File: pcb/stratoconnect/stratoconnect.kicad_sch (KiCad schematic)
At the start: 7 parts

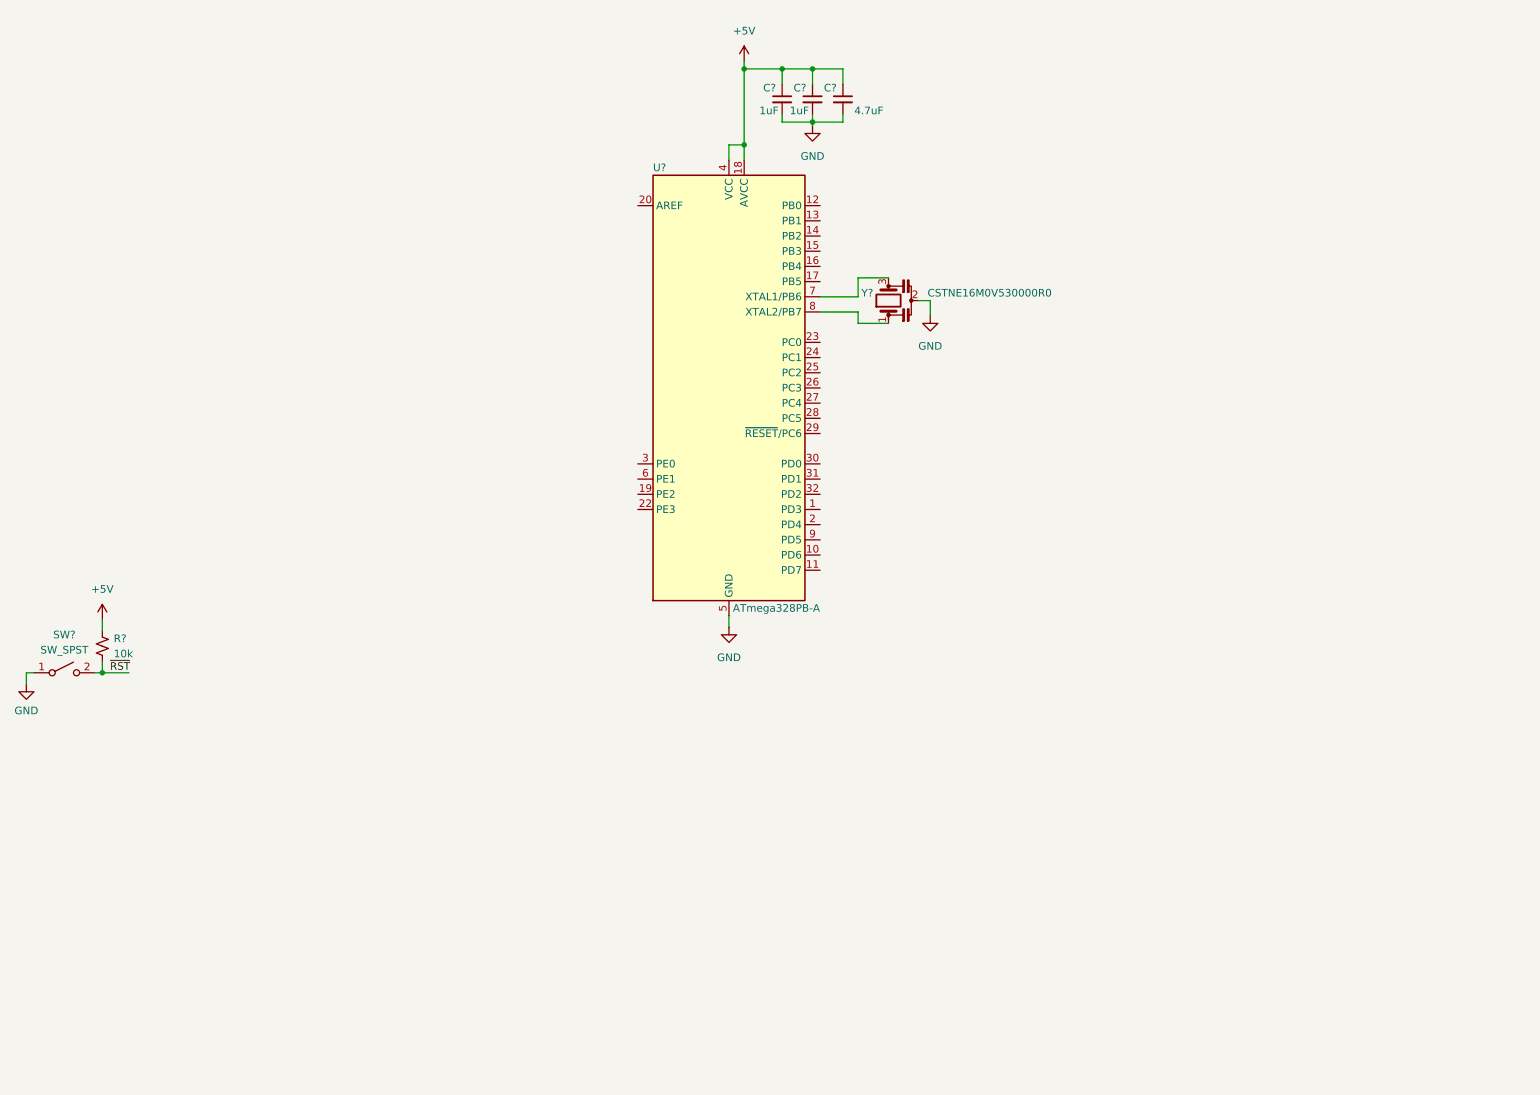
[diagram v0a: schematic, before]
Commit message: draw out the base schematic with the RF module
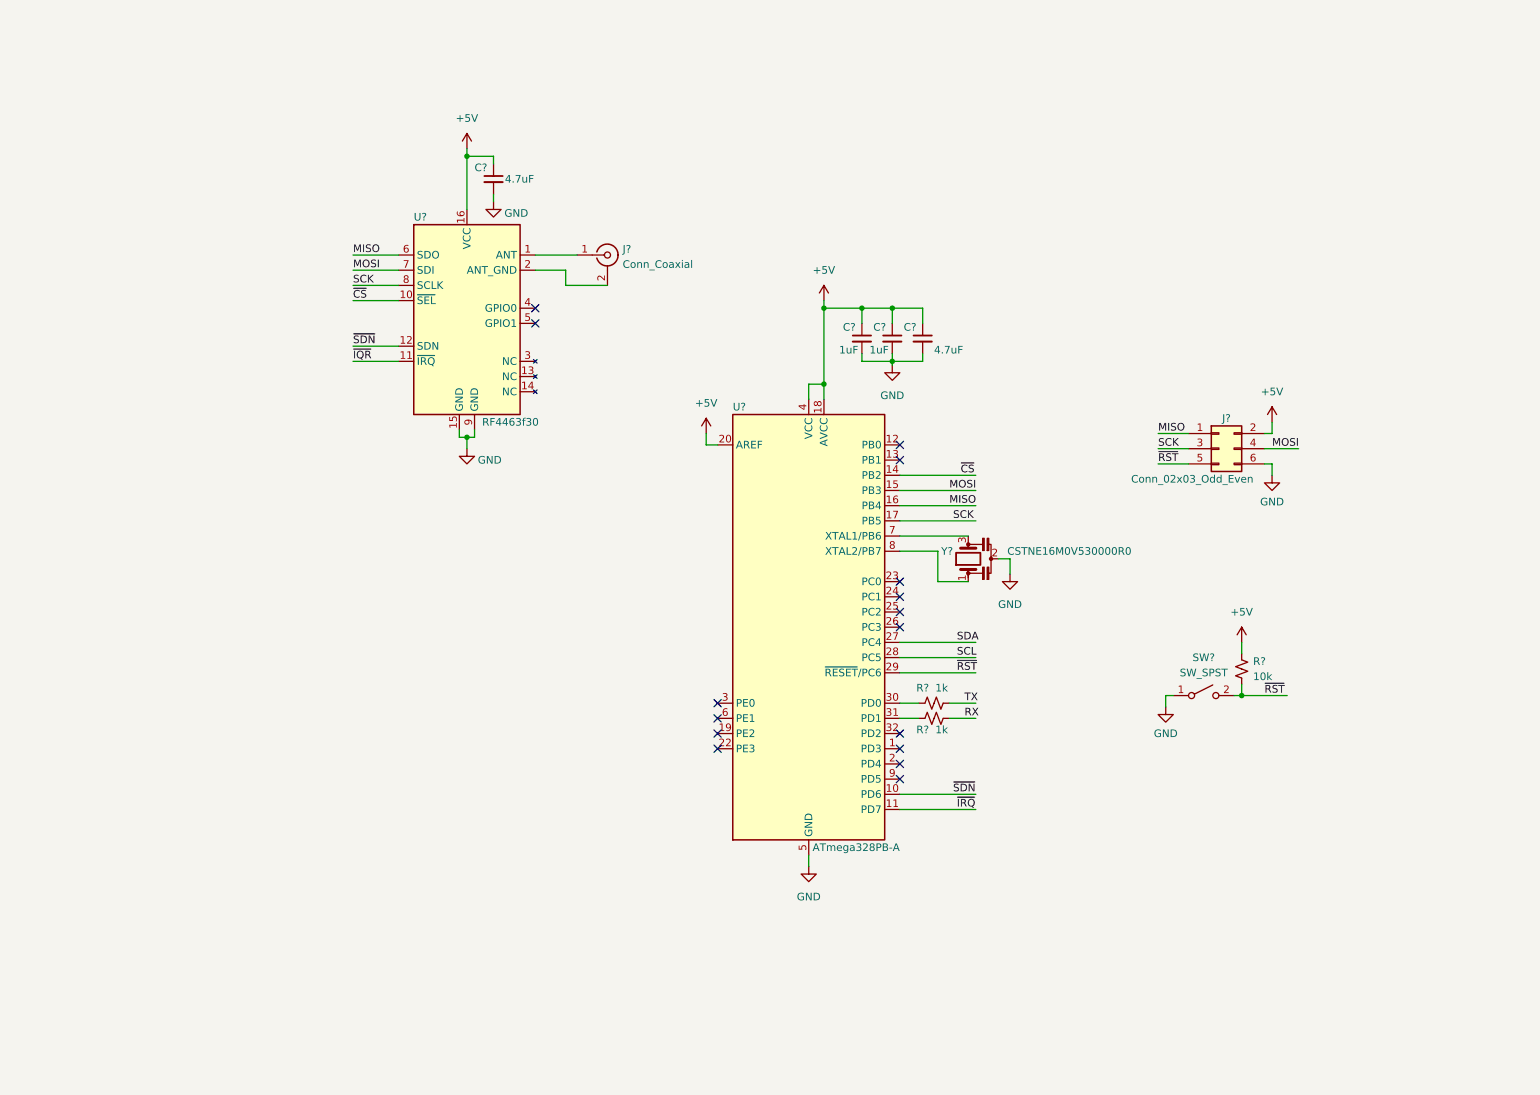
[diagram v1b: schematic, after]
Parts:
- added C?: 4.7uF, Capacitor_SMD:C_0603_1608Metric, symbol Device:C_Small
- added J?: Conn_02x03_Odd_Even, Connector_PinHeader_2.54mm:PinHeader_2x03_P2.54mm_Vertical, symbol Connector_Generic:Conn_02x03_Odd_Even
- added J?: Conn_Coaxial, symbol Connector:Conn_Coaxial
- added R? (x2): 1k, Resistor_SMD:R_0603_1608Metric, symbol Device:R_Small_US
- added U?: RF4463f30, RF:RF4463F30, symbol RF_Module:RF4463f30
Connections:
- net +5V: now also U?.20 (AREF), C?.1, J?.2 (Pin_2), U?.16 (VCC)
- net GND: now also C?.2, J?.6 (Pin_6), U?.15 (GND), U?.9 (GND)
- net ~{RST}: now also U?.29 (~{RESET}/PC6), J?.5 (Pin_5)
- net ~{SDN}: now reaches U?.10 (PD6)
- net ~{SDN}: now also U?.12 (SDN)
- net ~{IRQ}: now reaches U?.11 (PD7)
- net ~{CS}: now reaches U?.14 (PB2)
- net ~{CS}: now also U?.10 (~{SEL})
- net MOSI: now reaches U?.15 (PB3)
- net MOSI: now also J?.4 (Pin_4), U?.7 (SDI)
- net MISO: now reaches U?.16 (PB4)
- net MISO: now also J?.1 (Pin_1), U?.6 (SDO)
- net SCK: now reaches U?.17 (PB5)
- net SCK: now also J?.3 (Pin_3), U?.8 (SCLK)
- net SDA: now reaches U?.27 (PC4)
- net SCL: now reaches U?.28 (PC5)
- net at U?.30 (PD0): now also R?.1
- net at U?.31 (PD1): now also R?.1
- new net: J?.1 (In), U?.1 (ANT)
- new net: J?.2 (Ext), U?.2 (ANT_GND)
- new net RX: R?.2
- new net TX: R?.2
- new net ~{IQR}: U?.11 (~{IRQ})
- no-connect marks 0 -> 16
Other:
- moved on the sheet: C?, R?, SW?, U?, Y?

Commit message: add rough margin
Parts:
- added J3: Conn_01x05_Male, Connector_JST:JST_GH_BM05B-GHS-TBT_1x05-1MP_P1.25mm_Vertical, symbol Connector:Conn_01x05_Male
- added J4: Conn_01x02_Male, Connector_JST:JST_EH_S2B-EH_1x02_P2.50mm_Horizontal, symbol Connector:Conn_01x02_Male
- added J5: Conn_01x03_Male, Connector_JST:JST_GH_BM03B-GHS-TBT_1x03-1MP_P1.25mm_Vertical, symbol Connector:Conn_01x03_Male
- J1: renamed from J?; footprint (none) -> Connector_Coaxial:SMA_Molex_73251-2120_EdgeMount_Horizontal
- gave numbers to parts that had none: 12
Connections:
- net +5V: now also J4.1 (Pin_1)
- net GND: now also J3.5 (Pin_5), J4.2 (Pin_2), J5.2 (Pin_2)
- net RX: now also J5.1 (Pin_1)
- net SCL: now also J3.2 (Pin_2)
- net SDA: now also J3.3 (Pin_3)
- net TX: now also J5.3 (Pin_3)
- new net +3V3: J3.4 (Pin_4)
- new net ~{INT}: J3.1 (Pin_1)

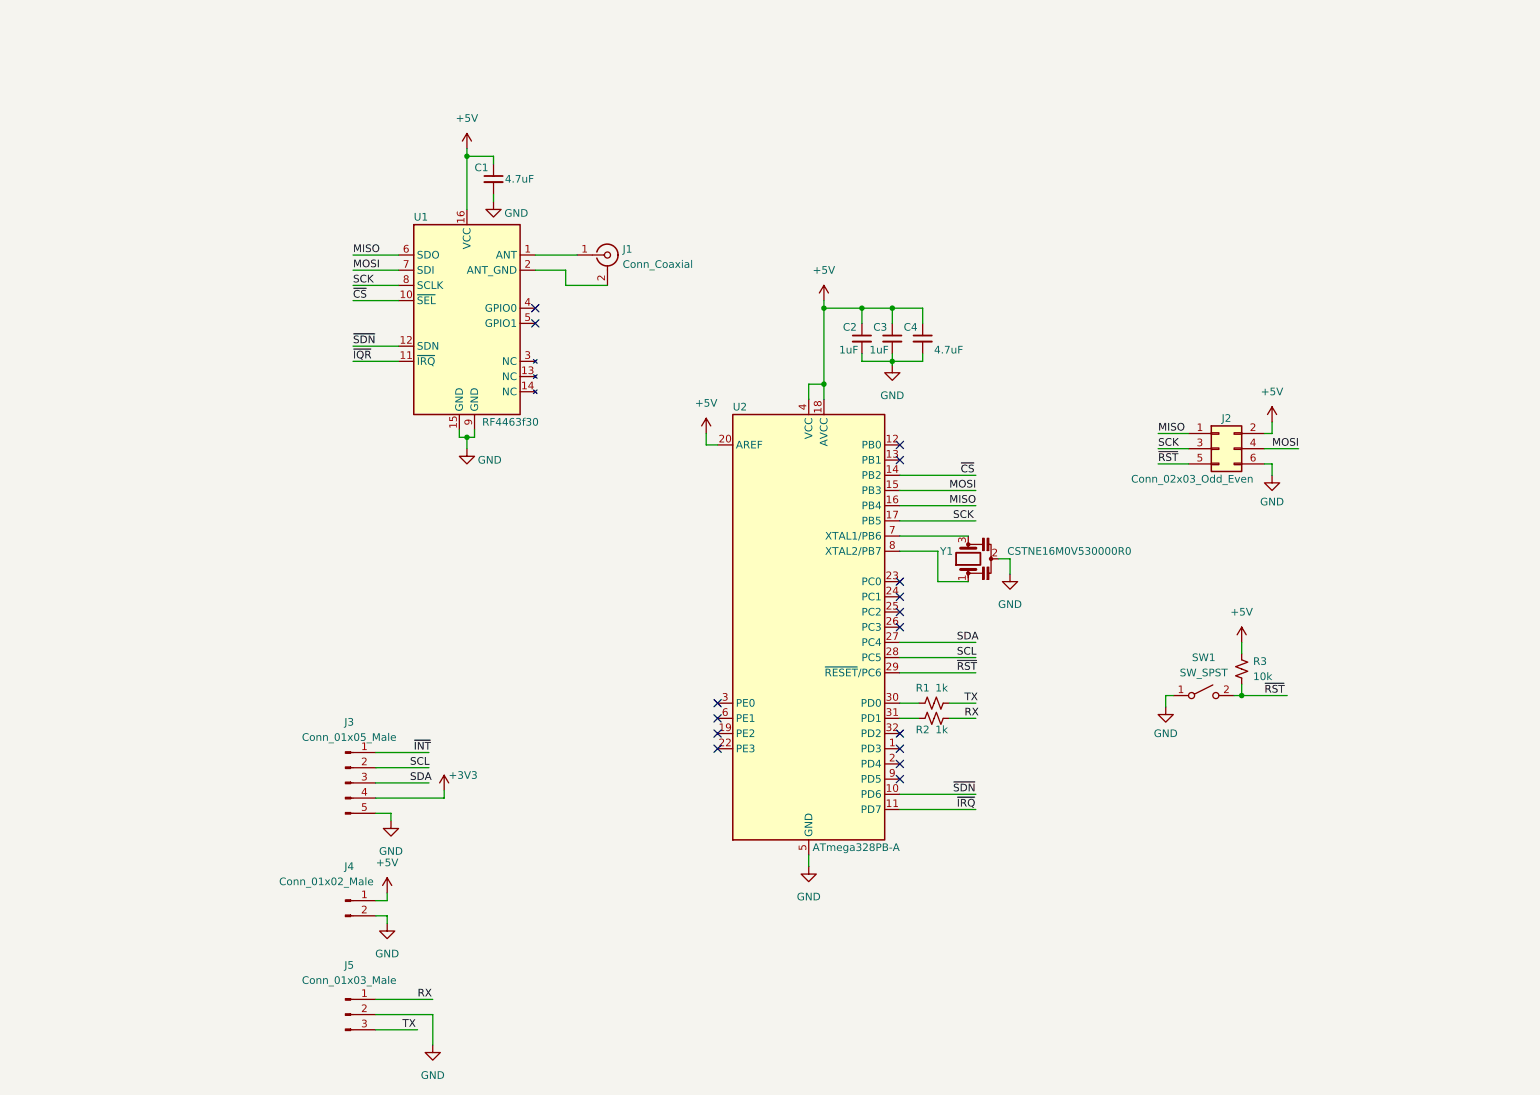
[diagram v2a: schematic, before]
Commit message: finish the shcematic, need to adjust component packages for headers, inductors and some of the resistors
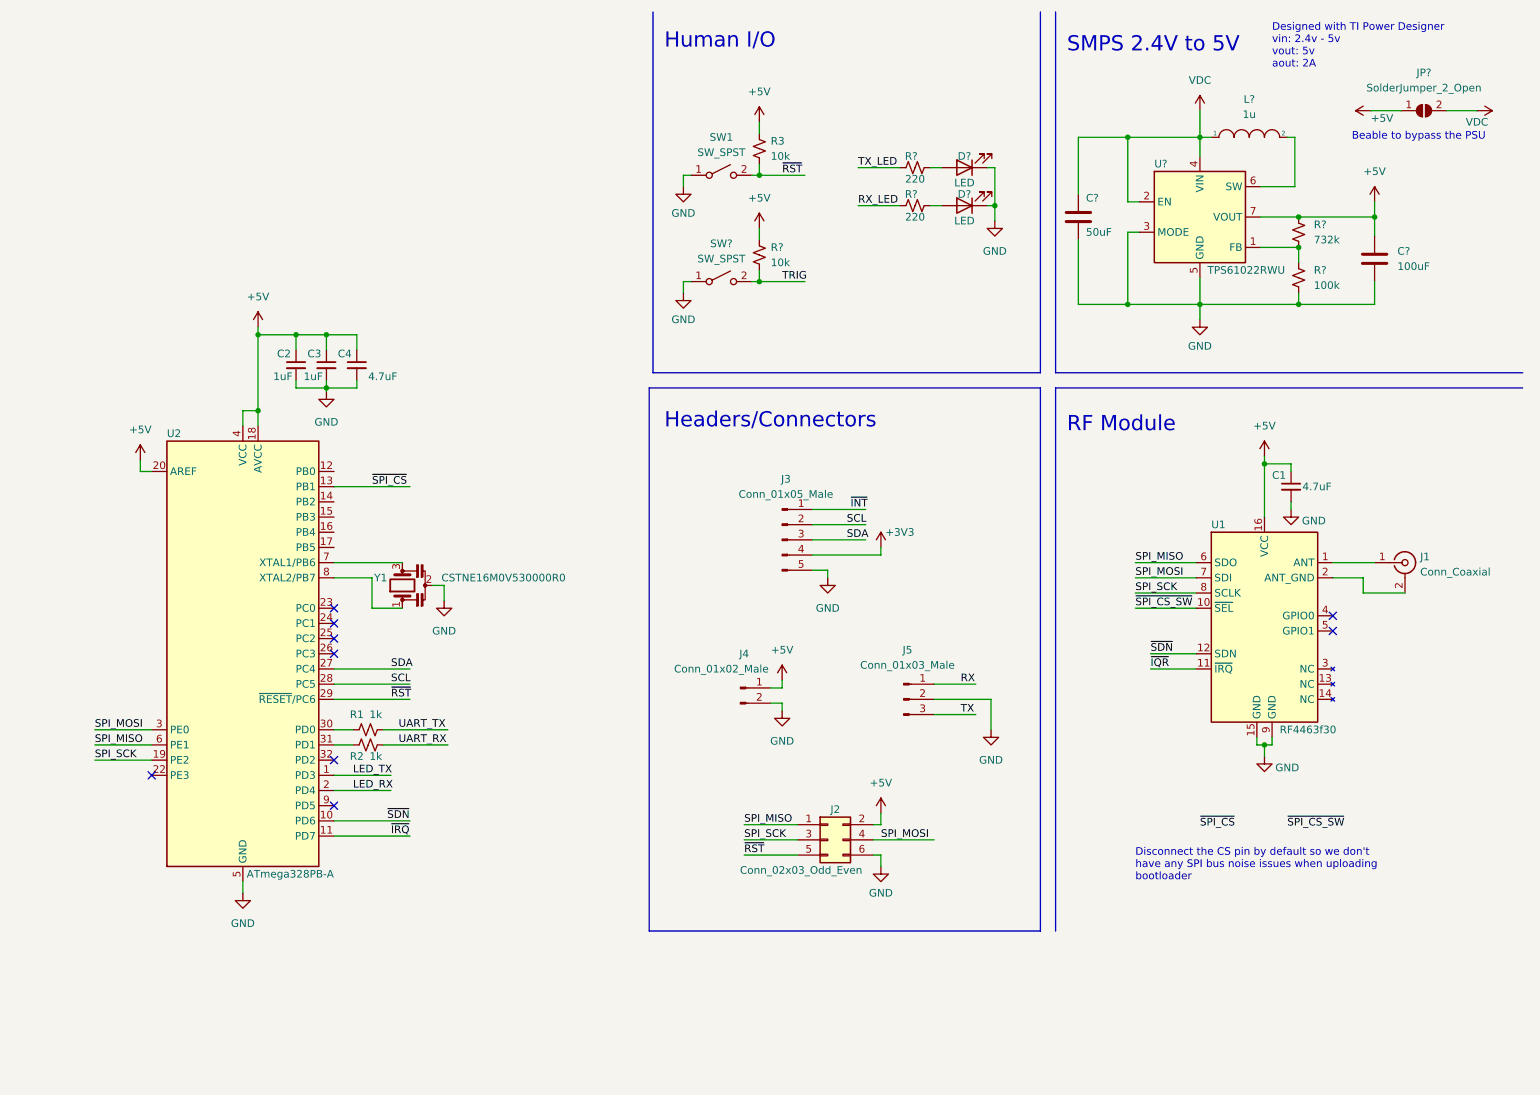
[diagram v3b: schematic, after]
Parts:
- added C?: 100uF, symbol Device:C
- added C?: 50uF, symbol Device:C
- added D? (x2): LED, LED_SMD:LED_0805_2012Metric, symbol Device:LED
- added JP?: SolderJumper_2_Open, symbol Jumper:SolderJumper_2_Open
- added L?: 1u, symbol pspice:INDUCTOR
- added R? (x2): 220, Resistor_SMD:R_0603_1608Metric, symbol Device:R_Small_US
- added R?: 732k, Resistor_SMD:R_0805_2012Metric, symbol Device:R_Small_US
- added R?: 10k, Resistor_SMD:R_0603_1608Metric, symbol Device:R_Small_US
- added R?: 100k, symbol Device:R_Small_US
- added SW?: SW_SPST, Button_Switch_SMD:SW_Push_1P1T_NO_CK_KMR2, symbol Switch:SW_SPST
- added U?: TPS61022RWU, Package_SON:WSON-8-1EP_2x2mm_P0.5mm_EP0.9x1.6mm, symbol Regulator_Switching:TPS61022RWU
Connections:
- net +5V: now also C?.1, JP?.1 (A), R?.1, R?.1, U?.7 (VOUT)
- net GND: now also C?.2, C?.2, D?.1 (K), D?.1 (K), R?.2, SW?.1 (A), U?.3 (MODE), U?.5 (GND)
- net RX: no longer R2.2
- net TX: no longer R1.2
- net LED_TX: now reaches U2.1 (PD3)
- net ~{SPI_CS}: now reaches U2.13 (PB1)
- net SPI_SCK: now reaches U2.19 (PE2)
- net SPI_SCK: now also J2.3 (Pin_3), U1.8 (SCLK)
- net LED_RX: now reaches U2.2 (PD4)
- net SPI_MOSI: now reaches U2.3 (PE0)
- net SPI_MOSI: now also J2.4 (Pin_4), U1.7 (SDI)
- net SPI_MISO: now reaches U2.6 (PE1)
- net SPI_MISO: now also J2.1 (Pin_1), U1.6 (SDO)
- removed net MISO: J2.1 (Pin_1), U1.6 (SDO), U2.16 (PB4)
- removed net MOSI: J2.4 (Pin_4), U1.7 (SDI), U2.15 (PB3)
- removed net SCK: J2.3 (Pin_3), U1.8 (SCLK), U2.17 (PB5)
- net ~{CS}: no longer names the net of U2.14 (PB2)
- net ~{CS}: no longer U1.10 (~{SEL})
- new net: D?.2 (A), R?.2 (x2)
- new net: R?.1, R?.2, U?.1 (FB)
- new net: L?.2, U?.6 (SW)
- new net RX_LED: R?.1
- new net TRIG: R?.2, SW?.2 (B)
- new net TX_LED: R?.1
- new net UART_RX: R2.2
- new net UART_TX: R1.2
- new net VDC: C?.1, JP?.2 (B), L?.1, U?.2 (EN), U?.4 (VIN)
- new net ~{SPI_CS_SW}: U1.10 (~{SEL})
- no-connect marks 16 -> 9
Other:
- note added: "Beable to bypass the PSU"
- note added: "Designed with TI Power Designer vin: 2.4v - 5v vout: 5v aout: 2A"
- note added: "Disconnect the CS pin by default so we don't have any SPI bus noise issues when uploading bootloader"
- note added: "Headers/Connectors"
- note added: "Human I/O"
- note added: "RF Module"
- note added: "SMPS 2.4V to 5V"
- moved on the sheet: C1, C2, C3, C4, J1, J2, J3, J4, J5, R1, R2, R3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
